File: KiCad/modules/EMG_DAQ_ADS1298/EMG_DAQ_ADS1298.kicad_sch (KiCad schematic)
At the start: 31 parts, among them J1 Conn_01x01_Pin, J10 Conn_01x01_Pin, J12 Conn_01x01_Pin, J13 Conn_01x01_Pin, J14 Conn_01x01_Pin, J15 Conn_01x01_Pin, J16 Conn_01x01_Pin, J2 Conn_01x01_Pin, J3 Conn_01x01_Pin, J4 Conn_01x01_Pin, J5 Conn_01x01_Pin, J6 Conn_01x01_Pin, J7 Conn_01x01_Pin, J8 Conn_01x01_Pin, J9 Conn_01x01_Pin, U1 AP2112K-3.3TRG1, U3 ADS1298CZXGR, Y1 Crystal

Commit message: updated
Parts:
- removed C1, C2: 22pF, Capacitor_SMD:C_0402_1005Metric, symbol Device:C
- removed J1, J2, J3, J4, J5, J6: Conn_01x01_Pin, Connector_PinHeader_1.27mm:PinHeader_1x01_P1.27mm_Vertical, symbol Connector:Conn_01x01_Pin
- removed JP1: SolderJumper_2_Bridged, Jumper:SolderJumper-2_P1.3mm_Bridged2Bar_RoundedPad1.0x1.5mm, symbol Jumper:SolderJumper_2_Bridged
- removed U3: ADS1298CZXGR, 00_Custom:BGA64C80P8X8_800X800X145, symbol 00_custom:ADS1298CZXGR
- removed Y1: Crystal, Crystal:Crystal_SMD_HC49-SD, symbol Device:Crystal
- added C10: 1nF, Capacitor_SMD:C_0402_1005Metric, symbol Device:C
- added C11, C12: 1uF, Capacitor_SMD:C_0402_1005Metric, symbol Device:C
- added C13, C8: 10uF, Capacitor_SMD:C_0402_1005Metric, symbol Device:C
- added C14, C9: 100nF, Capacitor_SMD:C_0402_1005Metric, symbol Device:C
- added C15: 22uF, Capacitor_SMD:C_0402_1005Metric, symbol Device:C
- added J10, J11, J13, J14, J15, J17, J18, J19, J20, J21, J22, J23, J24, J9: Conn_01x01_Pin, Connector_Wire:SolderWirePad_1x01_SMD_1x2mm, symbol Connector:Conn_01x01_Pin
- added J25, J26: Conn_01x01_Pin, 00_custom-footprints:PinHeader_1x01_P1.27mm_Vertical, symbol Connector:Conn_01x01_Pin
- added SW1: TS-1088R-02026, 00_lcsc:SW-SMD_L3.9-W3.0-P4.45, symbol 00_lcsc:TS-1088R-02026
- added U2: ADS1298CZXGT, 00_lcsc:NFBGA-64_L8.0-W8.0-R8-C8-P0.80-TL, symbol 00_lcsc:ADS1298CZXGT
- C3, C5: value 100nF -> 1uF
- C4: value 1uF -> 100nF
- C6: value 1nF -> 100nF
- C7: value 100nF -> 1.5nF
- J10, J13, J14, J15, J6, J7, J8, J9: footprint Connector_PinHeader_1.27mm:PinHeader_1x01_P1.27mm_Vertical -> 00_custom-footprints:PinHeader_1x01_P1.27mm_Vertical
- J12, J16: footprint Connector_PinHeader_1.27mm:PinHeader_1x01_P1.27mm_Vertical -> Connector_Wire:SolderWirePad_1x01_SMD_1x2mm
- R1: value 10K -> 1M
- R2: value 10M -> 10K
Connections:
- net GNDA is gone; now on net +3.3V: C3.2
- net RLDREF is gone; now on net BIAS_OUT: C7.1
- net cvref is gone; now on net GND: C4.1
- net +3.3V: now also C4.2, R2.2, U2.A4 (AVDD), U2.B4 (AVDD), U2.B8 (CLKSEL), U2.C8 (DVDD), U2.D8 (DVDD), U2.G5 (~{PWDN}); no longer C5.1
- net +3.3VA: now also C8.1, C9.1, U2.A6 (AVDD), U2.A7 (AVDD1), U2.B6 (AVDD), U2.C6 (AVDD); no longer C3.1
- net CSB: now also U2.F7 (CS)
- net GND: now also C3.1, C6.2, C10.2, C11.2, C12.2, C13.2, C14.2, C15.2, C8.2, C9.2, SW1.2, U2.A5 (AVSS), U2.A8 (AVSS1), U2.B5 (AVSS), U2.C5 (AVSS), U2.C7 (DGND), U2.D4 (AVSS), U2.D5 (AVSS), U2.D7 (DGND), U2.E4 (RESV1), U2.F6 (DAISY_IN), U2.G7 (START), U2.H4 (VREFN), U2.H7 (DGND); no longer C4.2, C7.2
- net MISO: now also U2.E8 (DOUT)
- net MOSI: now also U2.H8 (DIN)
- net SCLK: now also U2.F8 (SCLK)
- net extRef: now also U2.F3 (TESTN_PACE_OUT2)
- net in5+: now reaches J12.1 (Pin_1)
- net in5+: now also U2.D1 (IN5P)
- net in1+: now reaches J16.1 (Pin_1)
- net in1+: now also U2.H1 (IN1P)
- net CMOUT renamed BIAS_OUT
- net BIAS_OUT: now also J26.1 (Pin_1), U2.B3 (RLDOUT)
- removed net RLDINV: C6.1, R1.1, R2.1
- removed net RLDOUT: C6.2, R2.2
- new net BIAS_INV: C7.2, R1.1, U2.C3 (RLDINV)
- new net RESET: R2.1, SW1.1, U2.G6 (~{RESET})
- new net Refp: J25.1 (Pin_1), U2.E3 (TESTP_PACE_OUT1)
- new net VCAP1: C15.1, U2.H5 (VCAP1)
- new net VCAP2: C12.1, U2.H6 (VCAP2)
- new net VCAP3: C5.1, C6.1, U2.B7 (VCAP3)
- new net VCAP4: C11.1, U2.G3 (VCAP4)
- new net VREFP: C13.1, C14.1, U2.H3 (VREFP)
- new net WCT: C10.1, U2.D3 (WCT)
- new net in1-: J24.1 (Pin_1), U2.H2 (IN1N)
- new net in2+: J15.1 (Pin_1), U2.G1 (IN2P)
- new net in2-: J23.1 (Pin_1), U2.G2 (IN2N)
- new net in3+: J14.1 (Pin_1), U2.F1 (IN3P)
- new net in3-: J22.1 (Pin_1), U2.F2 (IN3N)
- new net in4+: J13.1 (Pin_1), U2.E1 (IN4P)
- new net in4-: J21.1 (Pin_1), U2.E2 (IN4N)
- new net in5-: J20.1 (Pin_1), U2.D2 (IN5N)
- new net in6+: J11.1 (Pin_1), U2.C1 (IN6P)
- new net in6-: J19.1 (Pin_1), U2.C2 (IN6N)
- new net in7+: J10.1 (Pin_1), U2.B1 (IN7P)
- new net in7-: J18.1 (Pin_1), U2.B2 (IN7N)
- new net in8+: J9.1 (Pin_1), U2.A1 (IN8P)
- new net in8-: J17.1 (Pin_1), U2.A2 (IN8N)
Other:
- moved on the sheet: C5, J10, J13, J14, J15, J6, J7, J8, J9, U1

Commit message: INA331 IMUICM
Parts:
- J10, J11, J12, J13, J14, J15, J16, J17, J18, J19, J20, J21, J22, J23, J24, J9: footprint Connector_Wire:SolderWirePad_1x01_SMD_1x2mm -> 00_custom-footprints:SolderWirePad_1x01_SMD_1x2mm
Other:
- moved on the sheet: C10, C11, C12, C13, C14, C15, C3, C4, C5, C6, C7, C8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

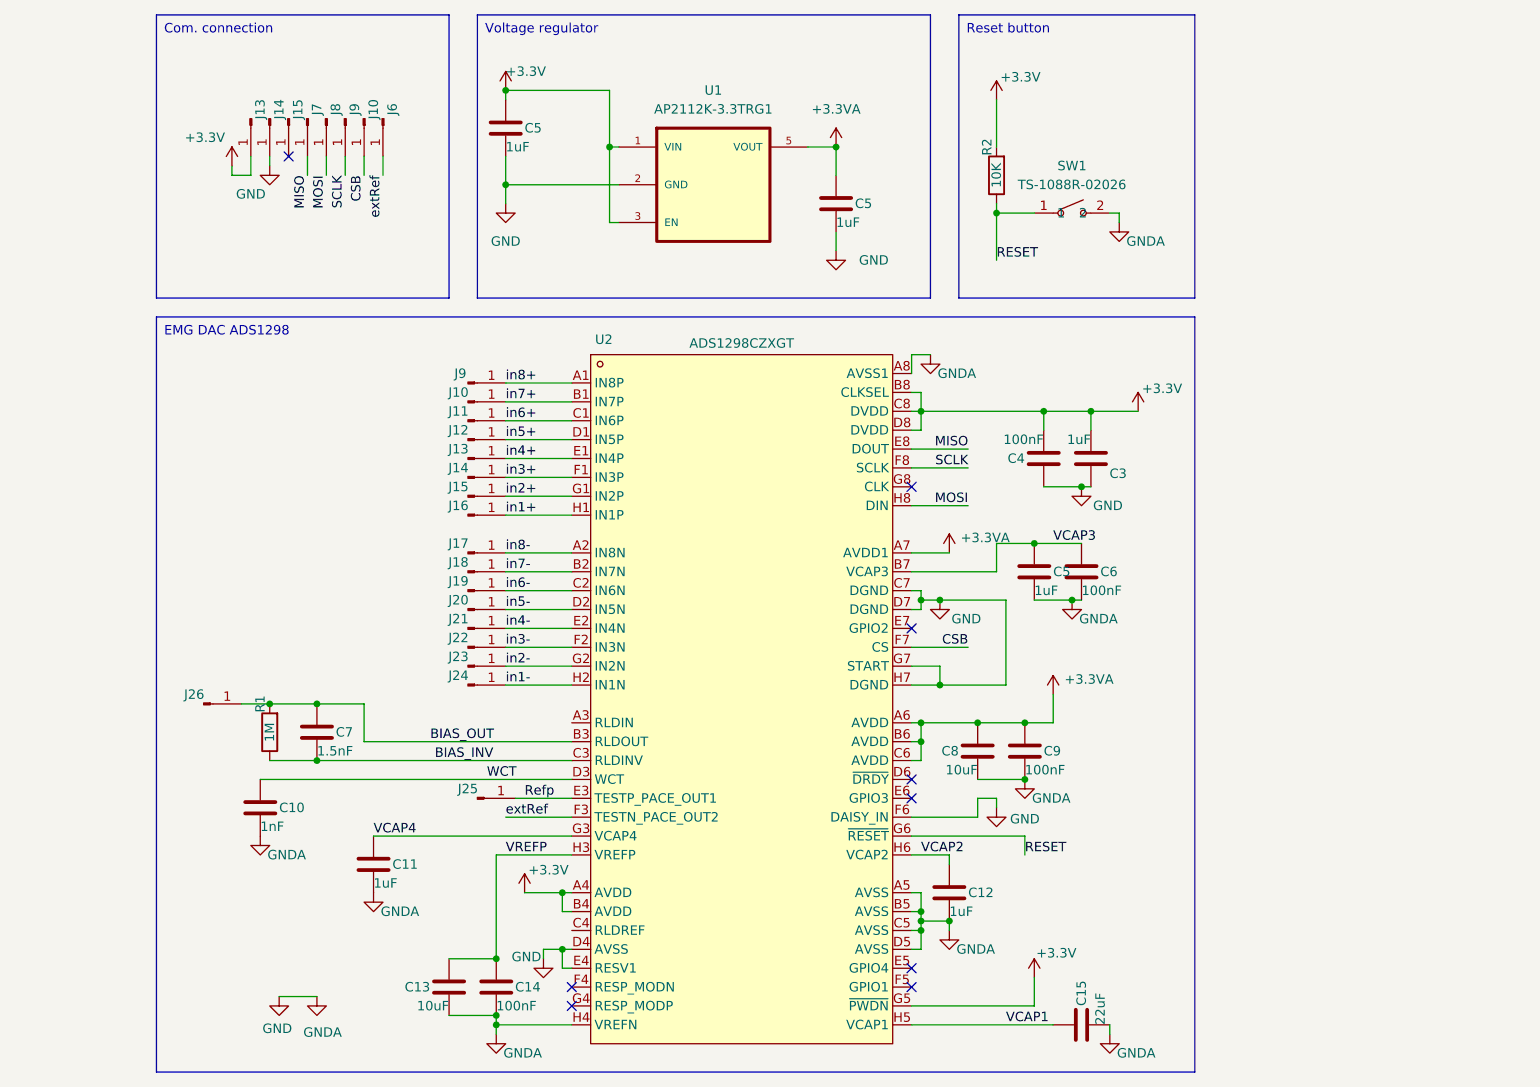
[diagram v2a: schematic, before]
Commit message: refactor and fixing most of the modules
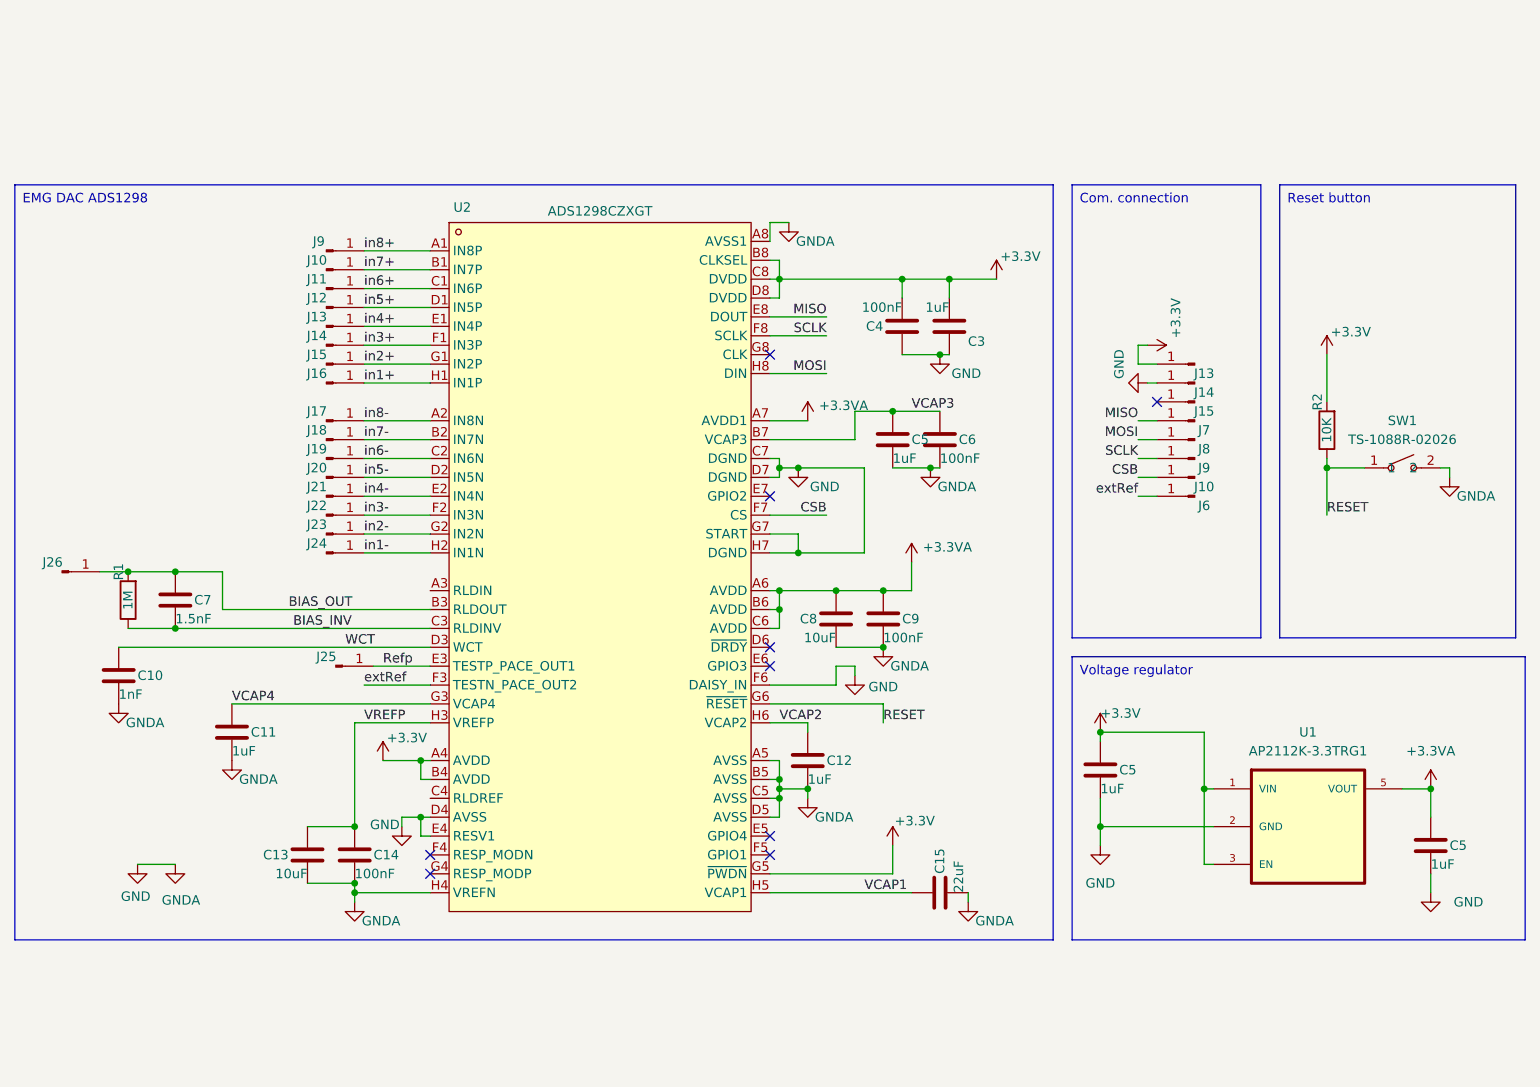
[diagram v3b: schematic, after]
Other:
- company: (none) -> Aightech
- title: (none) -> EMG ADS1298
- moved on the sheet: C10, C11, C12, C13, C14, C15, C3, C4, C5, C6, C7, C8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

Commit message: renamed SPI buses
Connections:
- net MISO renamed POCI
- net MOSI renamed PICO
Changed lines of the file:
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@@
 		)
 	)
-	(label "MOSI"
+	(label "PICO"
 		(at 198.12 77.47 180)
 		(fields_autoplaced yes)
@@
 		)
 	)
-	(label "MISO"
+	(label "POCI"
 		(at 156.21 60.96 180)
 		(fields_autoplaced yes)
@@
 		)
 	)
-	(label "MISO"
+	(label "POCI"
 		(at 198.12 74.93 180)
 		(fields_autoplaced yes)
@@
 		)
 	)
-	(label "MOSI"
+	(label "PICO"
 		(at 156.21 68.58 180)
 		(fields_autoplaced yes)
